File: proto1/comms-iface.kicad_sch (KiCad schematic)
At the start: 11 parts, among them J2 DIN-6, J3 DIN-6, Q1 AO3400A, Q2 AO3401A, Q3 AO3401A, Q4 AO3400A

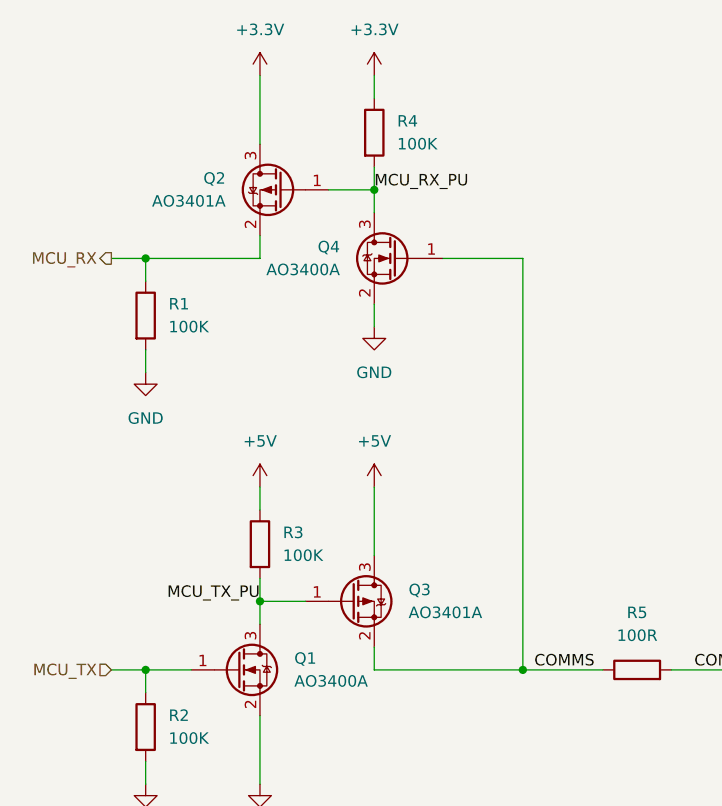
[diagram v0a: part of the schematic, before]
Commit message: proto1: Fix pfet orientation
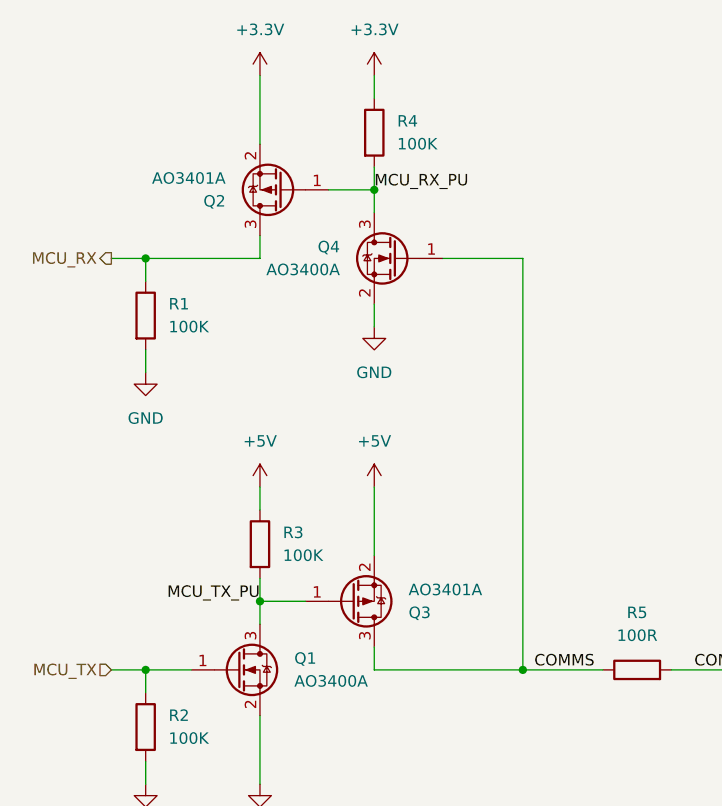
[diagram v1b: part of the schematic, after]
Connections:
- net +3.3V: now also Q2.2 (S); no longer Q2.3 (D)
- net +5V: now also Q3.2 (S); no longer Q3.3 (D)
- net COMMS: now also Q3.3 (D); no longer Q3.2 (S)
- net MCU_RX: now also Q2.3 (D); no longer Q2.2 (S)
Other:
- moved on the sheet: Q2
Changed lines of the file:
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@@
 	(symbol
 		(lib_id "Device:Q_PMOS_GSD")
-		(at 81.28 50.8 0)
-		(mirror y)
+		(at 81.28 50.8 180)
 		(unit 1)
 		(exclude_from_sim no)
@@
 		(dnp no)
 		(property "Reference" "Q2"
-			(at 74.93 49.5299 0)
+			(at 74.93 52.0701 0)
 			(effects
 				(font
@@
 		)
 		(property "Value" "AO3401A"
-			(at 74.93 52.0699 0)
+			(at 74.93 49.5301 0)
 			(effects
 				(font
@@
 		)
 		(property "Footprint" "Package_TO_SOT_SMD:SOT-23-3"
-			(at 76.2 48.26 0)
+			(at 76.2 53.34 0)
 			(effects
 				(font
@@
 		(lib_id "Device:Q_PMOS_GSD")
 		(at 88.9 96.52 0)
-		(unit 1)
-		(exclude_from_sim no)
-		(in_bom yes)
-		(on_board yes)
-		(dnp no)
-		(fields_autoplaced yes)
+		(mirror x)
+		(unit 1)
+		(exclude_from_sim no)
+		(in_bom yes)
+		(on_board yes)
+		(dnp no)
 		(property "Reference" "Q3"
-			(at 95.25 95.2499 0)
+			(at 95.25 97.7901 0)
 			(effects
 				(font
@@
 		)
 		(property "Value" "AO3401A"
-			(at 95.25 97.7899 0)
+			(at 95.25 95.2501 0)
 			(effects
 				(font
@@
 		)
 		(property "Footprint" "Package_TO_SOT_SMD:SOT-23-3"
-			(at 93.98 93.98 0)
-			(effects
-				(font
+			(at 93.98 99.06 0)
+			(effects
+				(font
